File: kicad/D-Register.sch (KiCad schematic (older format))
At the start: 19 parts, among them U119 74LS245, U120 74LS173, U121 74LS173

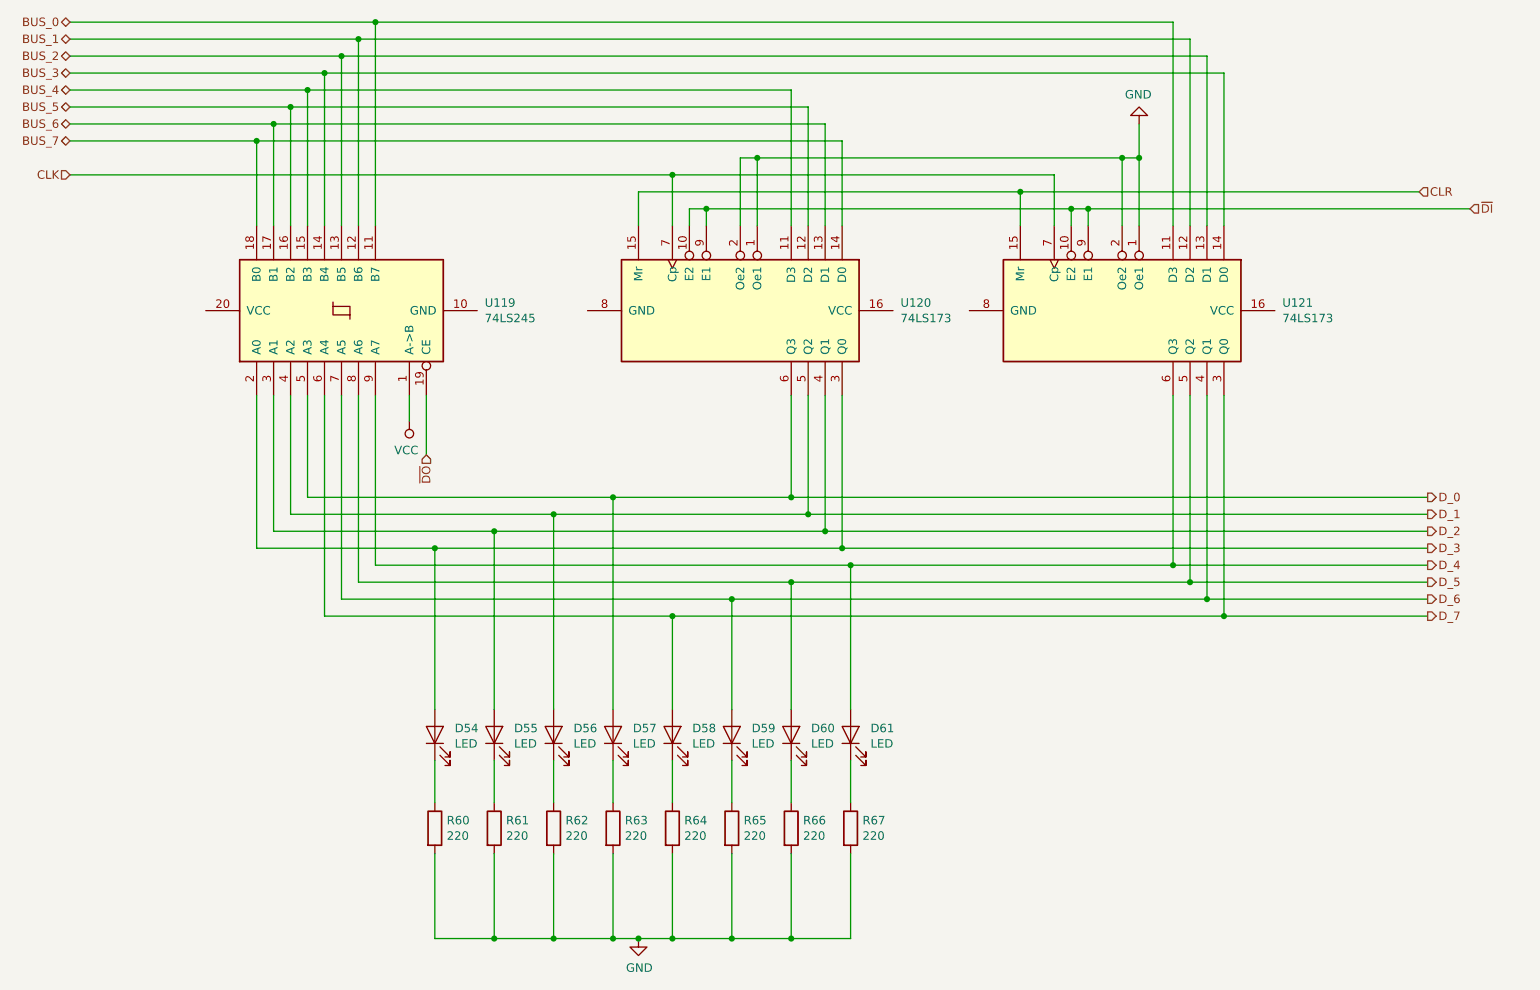
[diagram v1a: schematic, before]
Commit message: Reorganize part references
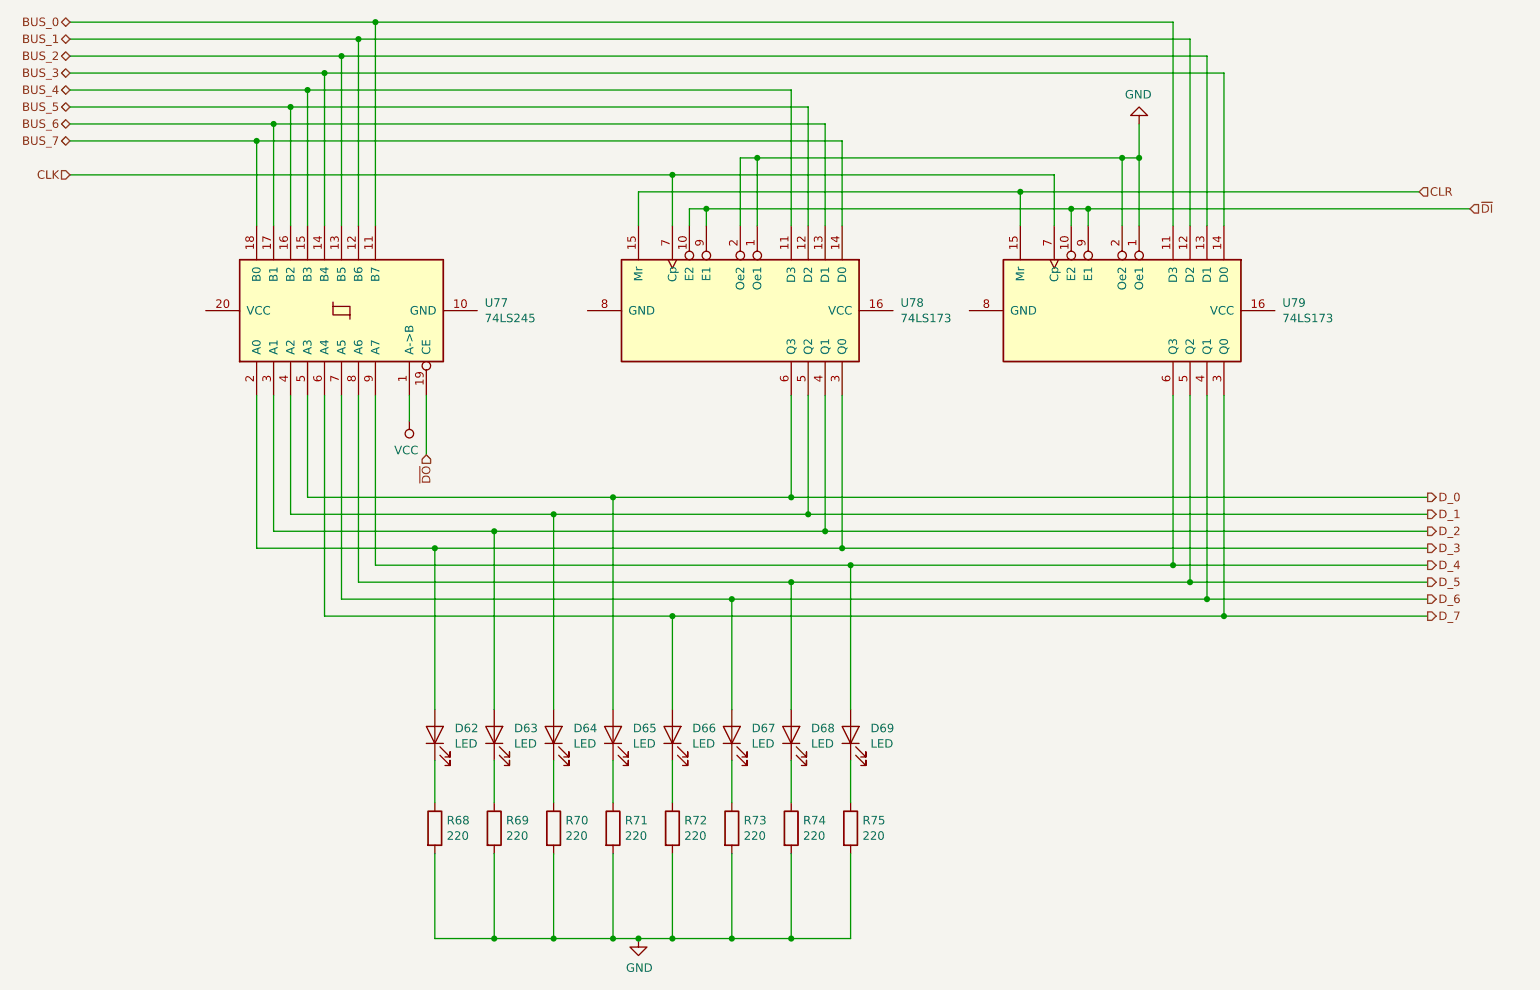
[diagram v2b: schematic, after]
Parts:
- renumbered D54 to D62, D55 to D63, D56 to D64, D57 to D65, D58 to D66, D59 to D67, D60 to D68, D61 to D69, R60 to R68, R61 to R69, R62 to R70, R63 to R71, R64 to R72, R65 to R73, R66 to R74, R67 to R75, U119 to U77, U120 to U78, U121 to U79
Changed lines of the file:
@@
 $Descr USLetter 11000 8500
 encoding utf-8
-Sheet 5 26
+Sheet 21 26
 Title "D Register"
 Date "2019-10-03"
@@
 AR Path="/5D9C73BD/5DA1765F" Ref="U?"  Part="1"
 AR Path="/5D9E82CE/5DA1765F" Ref="U?"  Part="1"
-AR Path="/5DA98D6D/5DA9A587/5DA1765F" Ref="U120"  Part="1"
-F 0 "U120" V 5204 4044 50  0000 L CNN
+AR Path="/5DA98D6D/5DA9A587/5DA1765F" Ref="U78"  Part="1"
+F 0 "U78" V 5204 4044 50  0000 L CNN
 F 1 "74LS173" V 5295 4044 50  0000 L CNN
 F 2 "" H 5250 3100 50  0001 C CNN
@@
 AR Path="/5D9C73BD/5DA1760E" Ref="R?"  Part="1"
 AR Path="/5D9E82CE/5DA1760E" Ref="R?"  Part="1"
-AR Path="/5DA98D6D/5DA9A587/5DA1760E" Ref="R67"  Part="1"
-F 0 "R67" H 5970 6196 50  0000 L CNN
+AR Path="/5DA98D6D/5DA9A587/5DA1760E" Ref="R75"  Part="1"
+F 0 "R75" H 5970 6196 50  0000 L CNN
 F 1 "220" H 5970 6105 50  0000 L CNN
 F 2 "" V 5830 6150 50  0001 C CNN
@@
 AR Path="/5D9C73BD/5DA17608" Ref="R?"  Part="1"
 AR Path="/5D9E82CE/5DA17608" Ref="R?"  Part="1"
-AR Path="/5DA98D6D/5DA9A587/5DA17608" Ref="R66"  Part="1"
-F 0 "R66" H 5620 6196 50  0000 L CNN
+AR Path="/5DA98D6D/5DA9A587/5DA17608" Ref="R74"  Part="1"
+F 0 "R74" H 5620 6196 50  0000 L CNN
 F 1 "220" H 5620 6105 50  0000 L CNN
 F 2 "" V 5480 6150 50  0001 C CNN
@@
 AR Path="/5D9C73BD/5DA17602" Ref="R?"  Part="1"
 AR Path="/5D9E82CE/5DA17602" Ref="R?"  Part="1"
-AR Path="/5DA98D6D/5DA9A587/5DA17602" Ref="R65"  Part="1"
-F 0 "R65" H 5270 6196 50  0000 L CNN
+AR Path="/5DA98D6D/5DA9A587/5DA17602" Ref="R73"  Part="1"
+F 0 "R73" H 5270 6196 50  0000 L CNN
 F 1 "220" H 5270 6105 50  0000 L CNN
 F 2 "" V 5130 6150 50  0001 C CNN
@@
 AR Path="/5D9C73BD/5DA175FC" Ref="R?"  Part="1"
 AR Path="/5D9E82CE/5DA175FC" Ref="R?"  Part="1"
-AR Path="/5DA98D6D/5DA9A587/5DA175FC" Ref="R64"  Part="1"
-F 0 "R64" H 4920 6196 50  0000 L CNN
+AR Path="/5DA98D6D/5DA9A587/5DA175FC" Ref="R72"  Part="1"
+F 0 "R72" H 4920 6196 50  0000 L CNN
 F 1 "220" H 4920 6105 50  0000 L CNN
 F 2 "" V 4780 6150 50  0001 C CNN
@@
 AR Path="/5D9C73BD/5DA175F6" Ref="R?"  Part="1"
 AR Path="/5D9E82CE/5DA175F6" Ref="R?"  Part="1"
-AR Path="/5DA98D6D/5DA9A587/5DA175F6" Ref="R63"  Part="1"
-F 0 "R63" H 4570 6196 50  0000 L CNN
+AR Path="/5DA98D6D/5DA9A587/5DA175F6" Ref="R71"  Part="1"
+F 0 "R71" H 4570 6196 50  0000 L CNN
 F 1 "220" H 4570 6105 50  0000 L CNN
 F 2 "" V 4430 6150 50  0001 C CNN
@@
 AR Path="/5D9C73BD/5DA175F0" Ref="R?"  Part="1"
 AR Path="/5D9E82CE/5DA175F0" Ref="R?"  Part="1"
-AR Path="/5DA98D6D/5DA9A587/5DA175F0" Ref="R62"  Part="1"
-F 0 "R62" H 4220 6196 50  0000 L CNN
+AR Path="/5DA98D6D/5DA9A587/5DA175F0" Ref="R70"  Part="1"
+F 0 "R70" H 4220 6196 50  0000 L CNN
 F 1 "220" H 4220 6105 50  0000 L CNN
 F 2 "" V 4080 6150 50  0001 C CNN
@@
 AR Path="/5D9C73BD/5DA175EA" Ref="R?"  Part="1"
 AR Path="/5D9E82CE/5DA175EA" Ref="R?"  Part="1"
-AR Path="/5DA98D6D/5DA9A587/5DA175EA" Ref="R61"  Part="1"
-F 0 "R61" H 3870 6196 50  0000 L CNN
+AR Path="/5DA98D6D/5DA9A587/5DA175EA" Ref="R69"  Part="1"
+F 0 "R69" H 3870 6196 50  0000 L CNN
 F 1 "220" H 3870 6105 50  0000 L CNN
 F 2 "" V 3730 6150 50  0001 C CNN
@@
 AR Path="/5D9C73BD/5DA175E4" Ref="R?"  Part="1"
 AR Path="/5D9E82CE/5DA175E4" Ref="R?"  Part="1"
-AR Path="/5DA98D6D/5DA9A587/5DA175E4" Ref="R60"  Part="1"
-F 0 "R60" H 3520 6196 50  0000 L CNN
+AR Path="/5DA98D6D/5DA9A587/5DA175E4" Ref="R68"  Part="1"
+F 0 "R68" H 3520 6196 50  0000 L CNN
 F 1 "220" H 3520 6105 50  0000 L CNN
 F 2 "" V 3380 6150 50  0001 C CNN
@@
 AR Path="/5D9C73BD/5DA175C8" Ref="D?"  Part="1"
 AR Path="/5D9E82CE/5DA175C8" Ref="D?"  Part="1"
-AR Path="/5DA98D6D/5DA9A587/5DA175C8" Ref="D61"  Part="1"
-F 0 "D61" V 5939 5483 50  0000 R CNN
+AR Path="/5DA98D6D/5DA9A587/5DA175C8" Ref="D69"  Part="1"
+F 0 "D69" V 5939 5483 50  0000 R CNN
 F 1 "LED" V 5848 5483 50  0000 R CNN
 F 2 "" H 5900 5600 50  0001 C CNN
@@
 AR Path="/5D9C73BD/5DA175C2" Ref="D?"  Part="1"
 AR Path="/5D9E82CE/5DA175C2" Ref="D?"  Part="1"
-AR Path="/5DA98D6D/5DA9A587/5DA175C2" Ref="D60"  Part="1"
-F 0 "D60" V 5589 5483 50  0000 R CNN
+AR Path="/5DA98D6D/5DA9A587/5DA175C2" Ref="D68"  Part="1"
+F 0 "D68" V 5589 5483 50  0000 R CNN
 F 1 "LED" V 5498 5483 50  0000 R CNN
 F 2 "" H 5550 5600 50  0001 C CNN
@@
 AR Path="/5D9C73BD/5DA175BC" Ref="D?"  Part="1"
 AR Path="/5D9E82CE/5DA175BC" Ref="D?"  Part="1"
-AR Path="/5DA98D6D/5DA9A587/5DA175BC" Ref="D59"  Part="1"
-F 0 "D59" V 5239 5483 50  0000 R CNN
+AR Path="/5DA98D6D/5DA9A587/5DA175BC" Ref="D67"  Part="1"
+F 0 "D67" V 5239 5483 50  0000 R CNN
 F 1 "LED" V 5148 5483 50  0000 R CNN
 F 2 "" H 5200 5600 50  0001 C CNN
@@
 AR Path="/5D9C73BD/5DA175B6" Ref="D?"  Part="1"
 AR Path="/5D9E82CE/5DA175B6" Ref="D?"  Part="1"
-AR Path="/5DA98D6D/5DA9A587/5DA175B6" Ref="D58"  Part="1"
-F 0 "D58" V 4889 5483 50  0000 R CNN
+AR Path="/5DA98D6D/5DA9A587/5DA175B6" Ref="D66"  Part="1"
+F 0 "D66" V 4889 5483 50  0000 R CNN
 F 1 "LED" V 4798 5483 50  0000 R CNN
 F 2 "" H 4850 5600 50  0001 C CNN
@@
 AR Path="/5D9C73BD/5DA175B0" Ref="D?"  Part="1"
 AR Path="/5D9E82CE/5DA175B0" Ref="D?"  Part="1"
-AR Path="/5DA98D6D/5DA9A587/5DA175B0" Ref="D57"  Part="1"
-F 0 "D57" V 4539 5483 50  0000 R CNN
+AR Path="/5DA98D6D/5DA9A587/5DA175B0" Ref="D65"  Part="1"
+F 0 "D65" V 4539 5483 50  0000 R CNN
 F 1 "LED" V 4448 5483 50  0000 R CNN
 F 2 "" H 4500 5600 50  0001 C CNN
@@
 AR Path="/5D9C73BD/5DA175AA" Ref="D?"  Part="1"
 AR Path="/5D9E82CE/5DA175AA" Ref="D?"  Part="1"
-AR Path="/5DA98D6D/5DA9A587/5DA175AA" Ref="D56"  Part="1"
-F 0 "D56" V 4189 5483 50  0000 R CNN
+AR Path="/5DA98D6D/5DA9A587/5DA175AA" Ref="D64"  Part="1"
+F 0 "D64" V 4189 5483 50  0000 R CNN
 F 1 "LED" V 4098 5483 50  0000 R CNN
 F 2 "" H 4150 5600 50  0001 C CNN
@@
 AR Path="/5D9C73BD/5DA175A4" Ref="D?"  Part="1"
 AR Path="/5D9E82CE/5DA175A4" Ref="D?"  Part="1"
-AR Path="/5DA98D6D/5DA9A587/5DA175A4" Ref="D55"  Part="1"
-F 0 "D55" V 3839 5483 50  0000 R CNN
+AR Path="/5DA98D6D/5DA9A587/5DA175A4" Ref="D63"  Part="1"
+F 0 "D63" V 3839 5483 50  0000 R CNN
 F 1 "LED" V 3748 5483 50  0000 R CNN
 F 2 "" H 3800 5600 50  0001 C CNN
@@
 AR Path="/5D9C73BD/5DA1759E" Ref="D?"  Part="1"
 AR Path="/5D9E82CE/5DA1759E" Ref="D?"  Part="1"
-AR Path="/5DA98D6D/5DA9A587/5DA1759E" Ref="D54"  Part="1"
-F 0 "D54" V 3489 5483 50  0000 R CNN
+AR Path="/5DA98D6D/5DA9A587/5DA1759E" Ref="D62"  Part="1"
+F 0 "D62" V 3489 5483 50  0000 R CNN
 F 1 "LED" V 3398 5483 50  0000 R CNN
 F 2 "" H 3450 5600 50  0001 C CNN
@@
 AR Path="/5D9C73BD/5DA17574" Ref="U?"  Part="1"
 AR Path="/5D9E82CE/5DA17574" Ref="U?"  Part="1"
-AR Path="/5DA98D6D/5DA9A587/5DA17574" Ref="U121"  Part="1"
-F 0 "U121" V 7454 4044 50  0000 L CNN
+AR Path="/5DA98D6D/5DA9A587/5DA17574" Ref="U79"  Part="1"
+F 0 "U79" V 7454 4044 50  0000 L CNN
 F 1 "74LS173" V 7545 4044 50  0000 L CNN
 F 2 "" H 7500 3100 50  0001 C CNN
@@
 AR Path="/5D9C73BD/5DA17547" Ref="U?"  Part="1"
 AR Path="/5D9E82CE/5DA17547" Ref="U?"  Part="1"
-AR Path="/5DA98D6D/5DA9A587/5DA17547" Ref="U119"  Part="1"
-F 0 "U119" V 2946 2256 50  0000 R CNN
+AR Path="/5DA98D6D/5DA9A587/5DA17547" Ref="U77"  Part="1"
+F 0 "U77" V 2946 2256 50  0000 R CNN
 F 1 "74LS245" V 2855 2256 50  0000 R CNN
 F 2 "" H 2900 3100 50  0001 C CNN
